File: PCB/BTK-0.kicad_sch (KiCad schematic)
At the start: 110 parts, among them J1 USB_C_Receptacle_USB2.0_16P, J2 Battery, J3 Conn_01x16_Pin, J4 Conn_01x16_Socket, SW1 EN, SW10 1,2, SW11 2,2, SW12 3,2, SW13 4,2, SW14 5,2, SW15 6,2, SW16 1,3, SW17 2,3, SW18 3,3, SW19 4,3, SW2 BOOT, SW20 5,3, SW21 6,3, SW22 1,4, SW23 2,4, SW24 3,4, SW25 4,4, SW26 5,4, SW27 6,4, SW28 1,4, SW29 2,4, SW3 RotaryEncoder_Switch_MP, SW30 3,4, SW31 4,4, SW32 5,4, SW33 6,4, SW4 1,1, SW5 2,1, SW6 3,1, SW7 4,1, SW8 5,1, SW9 6,1, U1 NCP1117-3.3_SOT223, U2 NCP1117-3.3_SOT223, U3 USBLC6-2SC6, U4 ESP32-C6-MINI-1, U5 TVS1400DRV, U6 BQ24075RGT

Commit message: new switches kailh sockets
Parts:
- SW10, SW11, SW12, SW13, SW14, SW15, SW16, SW17, SW18, SW19, SW20, SW21, SW22, SW23, SW24, SW25, SW26, SW27, SW28, SW29, SW30, SW31, SW32, SW33, SW4, SW5, SW6, SW7, SW8, SW9: footprint kb_switch:SW_MX_reversible -> kb_switch:Kailh_socket_MX_reversible
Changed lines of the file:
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@@
 			)
 		)
-		(property "Footprint" "kb_switch:SW_MX_reversible"
+		(property "Footprint" "kb_switch:Kailh_socket_MX_reversible"
 			(at 66.04 185.42 0)
 			(hide yes)
@@
 			)
 		)
-		(property "Footprint" "kb_switch:SW_MX_reversible"
+		(property "Footprint" "kb_switch:Kailh_socket_MX_reversible"
 			(at 20.32 185.42 0)
 			(hide yes)
@@
 			)
 		)
-		(property "Footprint" "kb_switch:SW_MX_reversible"
+		(property "Footprint" "kb_switch:Kailh_socket_MX_reversible"
 			(at 96.52 185.42 0)
 			(hide yes)
@@
 			)
 		)
-		(property "Footprint" "kb_switch:SW_MX_reversible"
+		(property "Footprint" "kb_switch:Kailh_socket_MX_reversible"
 			(at 81.28 172.72 0)
 			(hide yes)
@@
 			)
 		)
-		(property "Footprint" "kb_switch:SW_MX_reversible"
+		(property "Footprint" "kb_switch:Kailh_socket_MX_reversible"
 			(at 81.28 185.42 0)
 			(hide yes)
@@
 			)
 		)
-		(property "Footprint" "kb_switch:SW_MX_reversible"
+		(property "Footprint" "kb_switch:Kailh_socket_MX_reversible"
 			(at 96.52 210.82 0)
 			(hide yes)
@@
 			)
 		)
-		(property "Footprint" "kb_switch:SW_MX_reversible"
+		(property "Footprint" "kb_switch:Kailh_socket_MX_reversible"
 			(at 50.8 210.82 0)
 			(hide yes)
@@
 			)
 		)
-		(property "Footprint" "kb_switch:SW_MX_reversible"
+		(property "Footprint" "kb_switch:Kailh_socket_MX_reversible"
 			(at 35.56 185.42 0)
 			(hide yes)
@@
 			)
 		)
-		(property "Footprint" "kb_switch:SW_MX_reversible"
+		(property "Footprint" "kb_switch:Kailh_socket_MX_reversible"
 			(at 50.8 172.72 0)
 			(hide yes)
@@
 			)
 		)
-		(property "Footprint" "kb_switch:SW_MX_reversible"
+		(property "Footprint" "kb_switch:Kailh_socket_MX_reversible"
 			(at 81.28 210.82 0)
 			(hide yes)
@@
 			)
 		)
-		(property "Footprint" "kb_switch:SW_MX_reversible"
+		(property "Footprint" "kb_switch:Kailh_socket_MX_reversible"
 			(at 50.8 223.52 0)
 			(hide yes)
@@
 			)
 		)
-		(property "Footprint" "kb_switch:SW_MX_reversible"
+		(property "Footprint" "kb_switch:Kailh_socket_MX_reversible"
 			(at 35.56 198.12 0)
 			(hide yes)
@@
 			)
 		)
-		(property "Footprint" "kb_switch:SW_MX_reversible"
+		(property "Footprint" "kb_switch:Kailh_socket_MX_reversible"
 			(at 96.52 223.52 0)
 			(hide yes)
@@
 			)
 		)
-		(property "Footprint" "kb_switch:SW_MX_reversible"
+		(property "Footprint" "kb_switch:Kailh_socket_MX_reversible"
 			(at 35.56 210.82 0)
 			(hide yes)
@@
 			)
 		)
-		(property "Footprint" "kb_switch:SW_MX_reversible"
+		(property "Footprint" "kb_switch:Kailh_socket_MX_reversible"
 			(at 20.32 223.52 0)
 			(hide yes)
@@
 			)
 		)
-		(property "Footprint" "kb_switch:SW_MX_reversible"
+		(property "Footprint" "kb_switch:Kailh_socket_MX_reversible"
 			(at 66.04 210.82 0)
 			(hide yes)
@@
 			)
 		)
-		(property "Footprint" "kb_switch:SW_MX_reversible"
+		(property "Footprint" "kb_switch:Kailh_socket_MX_reversible"
 			(at 20.32 172.72 0)
 			(hide yes)
@@
 			)
 		)
-		(property "Footprint" "kb_switch:SW_MX_reversible"
+		(property "Footprint" "kb_switch:Kailh_socket_MX_reversible"
 			(at 96.52 172.72 0)
 			(hide yes)
@@
 			)
 		)
-		(property "Footprint" "kb_switch:SW_MX_reversible"
+		(property "Footprint" "kb_switch:Kailh_socket_MX_reversible"
 			(at 35.56 223.52 0)
 			(hide yes)
@@
 			)
 		)
-		(property "Footprint" "kb_switch:SW_MX_reversible"
+		(property "Footprint" "kb_switch:Kailh_socket_MX_reversible"
 			(at 66.04 172.72 0)
 			(hide yes)
@@
 			)
 		)
-		(property "Footprint" "kb_switch:SW_MX_reversible"
+		(property "Footprint" "kb_switch:Kailh_socket_MX_reversible"
 			(at 96.52 198.12 0)
 			(hide yes)
@@
 			)
 		)
-		(property "Footprint" "kb_switch:SW_MX_reversible"
+		(property "Footprint" "kb_switch:Kailh_socket_MX_reversible"
 			(at 50.8 185.42 0)
 			(hide yes)
@@
 			)
 		)
-		(property "Footprint" "kb_switch:SW_MX_reversible"
+		(property "Footprint" "kb_switch:Kailh_socket_MX_reversible"
 			(at 66.04 223.52 0)
 			(hide yes)
@@
 			)
 		)
-		(property "Footprint" "kb_switch:SW_MX_reversible"
+		(property "Footprint" "kb_switch:Kailh_socket_MX_reversible"
 			(at 81.28 198.12 0)
 			(hide yes)
@@
 			)
 		)
-		(property "Footprint" "kb_switch:SW_MX_reversible"
+		(property "Footprint" "kb_switch:Kailh_socket_MX_reversible"
 			(at 20.32 198.12 0)
 			(hide yes)
@@
 			)
 		)
-		(property "Footprint" "kb_switch:SW_MX_reversible"
+		(property "Footprint" "kb_switch:Kailh_socket_MX_reversible"
 			(at 35.56 172.72 0)
 			(hide yes)
@@
 			)
 		)
-		(property "Footprint" "kb_switch:SW_MX_reversible"
+		(property "Footprint" "kb_switch:Kailh_socket_MX_reversible"
 			(at 50.8 198.12 0)
 			(hide yes)
@@
 			)
 		)
-		(property "Footprint" "kb_switch:SW_MX_reversible"
+		(property "Footprint" "kb_switch:Kailh_socket_MX_reversible"
 			(at 81.28 223.52 0)
 			(hide yes)
@@
 			)
 		)
-		(property "Footprint" "kb_switch:SW_MX_reversible"
+		(property "Footprint" "kb_switch:Kailh_socket_MX_reversible"
 			(at 20.32 210.82 0)
 			(hide yes)
@@
 			)
 		)
-		(property "Footprint" "kb_switch:SW_MX_reversible"
+		(property "Footprint" "kb_switch:Kailh_socket_MX_reversible"
 			(at 66.04 198.12 0)
 			(hide yes)

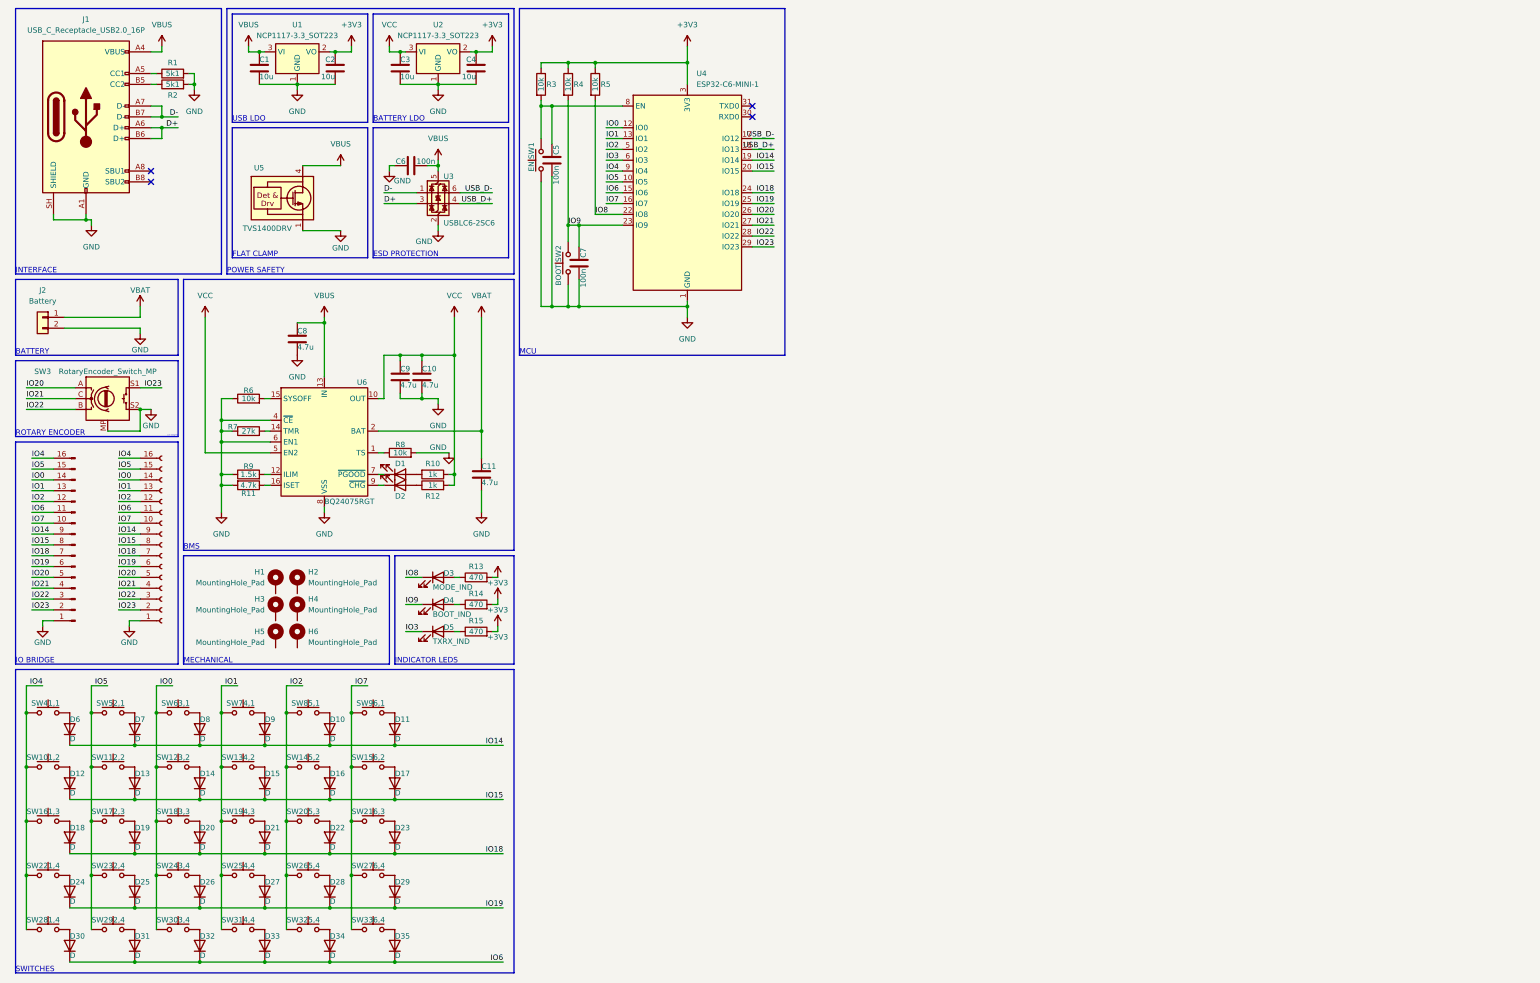
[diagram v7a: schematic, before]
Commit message: fixed rollback, alignment and powerswitch redone
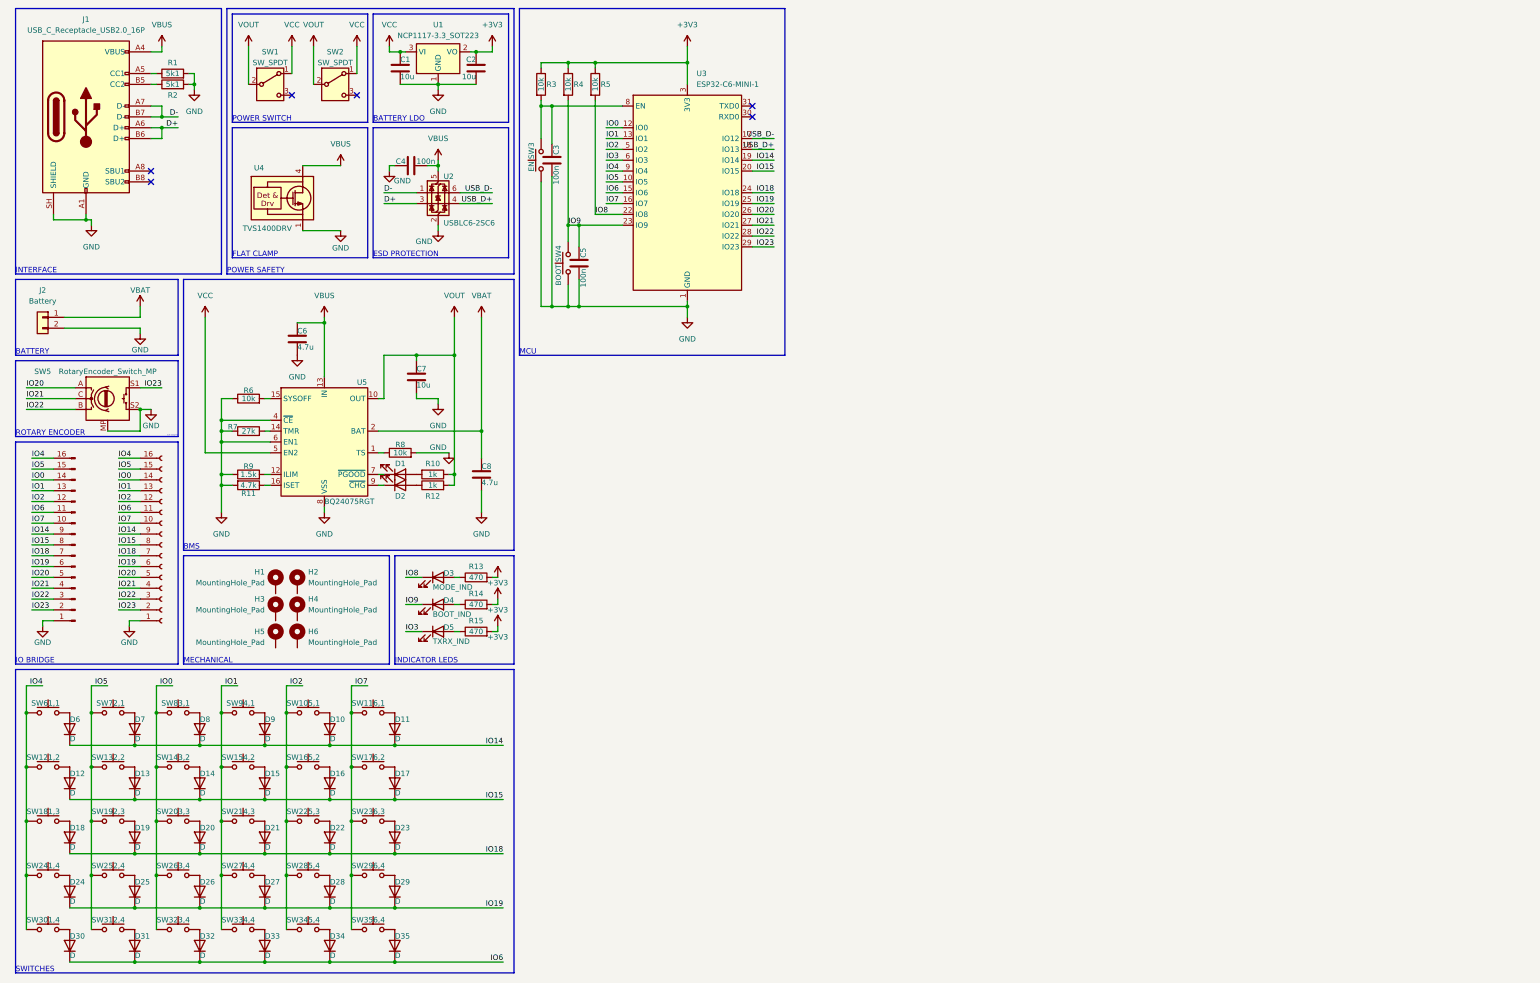
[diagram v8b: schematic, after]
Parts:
- removed C1, C2: 10u, Capacitor_SMD:C_0805_2012Metric, symbol Device:C
- removed C9: 4.7u, Capacitor_SMD:C_0805_2012Metric, symbol Device:C
- removed U1: NCP1117-3.3_SOT223, Package_TO_SOT_SMD:SOT-223-3_TabPin2, symbol Regulator_Linear:NCP1117-3.3_SOT223
- added SW1, SW2: SW_SPDT, JS102011SAQN:SW_JS102011SAQN, symbol Switch:SW_SPDT
- C7: renamed from C10; value 4.7u -> 10u
- renumbered C3 to C1, C4 to C2, C5 to C3, C6 to C4, C7 to C5, C8 to C6, C11 to C8, SW8 to SW10, SW9 to SW11, SW10 to SW12, SW11 to SW13, SW12 to SW14, SW13 to SW15, SW14 to SW16, SW15 to SW17, SW16 to SW18, SW17 to SW19, SW18 to SW20, SW19 to SW21, SW20 to SW22, SW21 to SW23, SW22 to SW24, SW23 to SW25, SW24 to SW26, SW25 to SW27, SW26 to SW28, SW27 to SW29, SW1 to SW3, SW28 to SW30, SW29 to SW31, SW30 to SW32, SW31 to SW33, SW32 to SW34, SW33 to SW35, SW2 to SW4, SW3 to SW5, SW4 to SW6, SW5 to SW7, SW6 to SW8, SW7 to SW9, U2 to U1, U3 to U2, U4 to U3, U5 to U4, U6 to U5
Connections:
- net VCC: now also SW1.1 (A), SW2.1 (A); no longer C7.1, R10.1, R12.2, U5.10 (OUT), U5.11 (OUT)
- new net VOUT: C7.1, R10.1, R12.2, SW1.2 (B), SW2.2 (B), U5.10 (OUT), U5.11 (OUT)
- no-connect marks 4 -> 6
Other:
- note added: "POWER SWITCH"
- note removed: "USB LDO"
- moved on the sheet: C7
